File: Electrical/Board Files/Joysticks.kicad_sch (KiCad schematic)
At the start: 8 parts

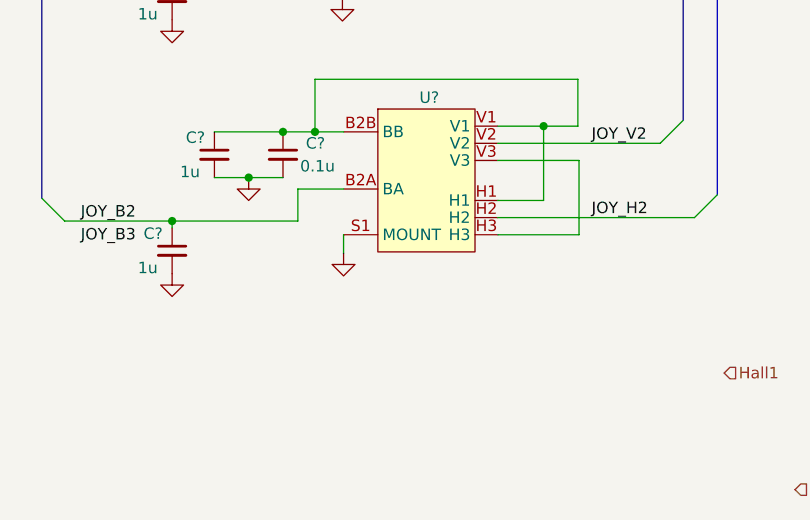
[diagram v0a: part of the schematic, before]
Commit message: Adding new block diagram
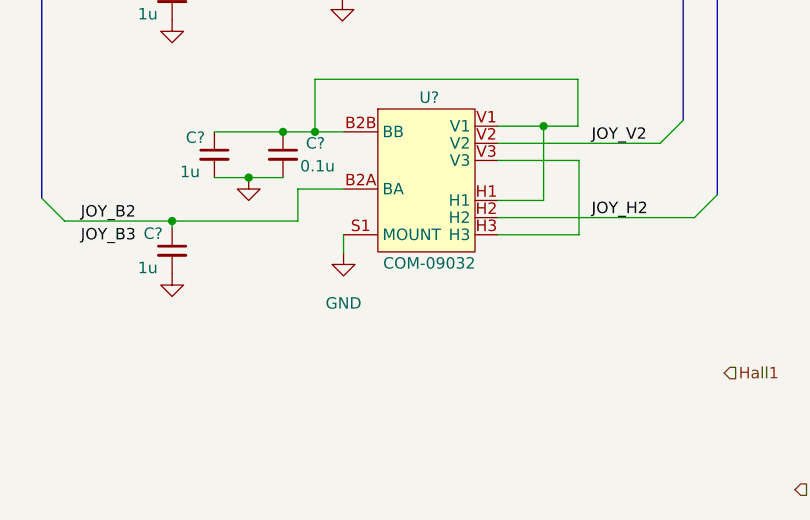
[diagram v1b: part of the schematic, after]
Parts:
- U?: value (none) -> COM-09032
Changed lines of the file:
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@@
       (effects (font (size 1.27 1.27)) hide)
     )
-    (property "Value" "" (id 1) (at 142.621 117.475 0))
+    (property "Value" "GND" (id 1) (at 142.621 117.475 0))
     (property "Footprint" "" (id 2) (at 142.621 111.887 0)
       (effects (font (size 1.27 1.27)) hide)
@@
     (in_bom yes) (on_board yes)
     (property "Reference" "U?" (id 0) (at 152.146 94.615 0))
-    (property "Value" "" (id 1) (at 152.146 113.03 0))
+    (property "Value" "COM-09032" (id 1) (at 152.146 113.03 0))
     (property "Footprint" "" (id 2) (at 152.146 102.87 0)
       (effects (font (size 1.27 1.27)) hide)

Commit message: Updating for 3v3 operation
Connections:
- net GND: now also U?.H3, U?.H3, U?.V3, U?.V3
- net +3V3: now reaches C?.1, C?.1, U?.B1B (S1), U?.B2B (BB), U?.H1, U?.V1
- net +3V3: now also C?.1, C?.1, U?.B1B (S1), U?.B2B (BB), U?.H1, U?.V1
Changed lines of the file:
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@@
   (junction (at 164.719 69.469) (diameter 0) (color 0 0 0 0)
   )
+  (junction (at 139.319 64.262) (diameter 0) (color 0 0 0 0)
+  )
+  (junction (at 168.783 109.855) (diameter 0) (color 0 0 0 0)
+  )
   (junction (at 139.446 98.425) (diameter 0) (color 0 0 0 0)
   )
@@
   )
   (junction (at 131.953 75.184) (diameter 0) (color 0 0 0 0)
+  )
+  (junction (at 139.446 92.583) (diameter 0) (color 0 0 0 0)
+  )
+  (junction (at 168.656 81.534) (diameter 0) (color 0 0 0 0)
   )
   (junction (at 135.763 70.104) (diameter 0) (color 0 0 0 0)
@@
     (effects (font (size 1.27 1.27)) (justify left bottom))
   )
-  (label "JOY_B3" (at 113.411 110.871 0)
-    (effects (font (size 1.27 1.27)) (justify left bottom))
-  )
   (label "JOY_V1" (at 170.18 71.374 0)
     (effects (font (size 1.27 1.27)) (justify left bottom))
@@
     (effects (font (size 1.27 1.27)) (justify left bottom))
   )
-  (hierarchical_label "JOY_H[1..2]" (shape input) (at 194.31 77.089 0)
+  (hierarchical_label "JOY_H[1..2]" (shape output) (at 194.31 77.089 0)
     (effects (font (size 1.27 1.27)) (justify left))
   )
-  (hierarchical_label "JOY_V[1..2]" (shape input) (at 194.31 68.834 0)
+  (hierarchical_label "JOY_V[1..2]" (shape output) (at 194.31 68.834 0)
     (effects (font (size 1.27 1.27)) (justify left))
   )
-  (hierarchical_label "hall2" (shape input) (at 192.786 138.176 0)
+  (hierarchical_label "hall2" (shape output) (at 192.786 138.176 0)
     (effects (font (size 1.27 1.27)) (justify left))
   )
-  (hierarchical_label "JOY_B[1..2]" (shape input) (at 106.045 77.47 180)
+  (hierarchical_label "JOY_B[1..2]" (shape output) (at 106.045 77.47 180)
     (effects (font (size 1.27 1.27)) (justify right))
   )
-  (hierarchical_label "Hall1" (shape input) (at 184.912 125.222 0)
+  (hierarchical_label "Hall1" (shape output) (at 184.912 125.222 0)
     (effects (font (size 1.27 1.27)) (justify left))
   )
@@
     (pin "1")
   )
+  (symbol (lib_id "power:+3V3") (at 139.446 92.583 0) (unit 1)
+    (in_bom yes) (on_board yes) (fields_autoplaced)
+    (property "Reference" "#PWR?" (id 0) (at 139.446 96.393 0)
+      (effects (font (size 1.27 1.27)) hide)
+    )
+    (property "Value" "+3V3" (id 1) (at 139.446 88.011 0))
+    (property "Footprint" "" (id 2) (at 139.446 92.583 0)
+      (effects (font (size 1.27 1.27)) hide)
+    )
+    (property "Datasheet" "" (id 3) (at 139.446 92.583 0)
+      (effects (font (size 1.27 1.27)) hide)
+    )
+    (pin "1")
+  )
   (symbol (lib_id "Device:C_Small") (at 123.571 111.633 0) (unit 1)
     (in_bom yes) (on_board yes)
@@
     (pin "2")
   )
+  (symbol (lib_id "power:GND") (at 168.656 81.534 0) (unit 1)
+    (in_bom yes) (on_board yes) (fields_autoplaced)
+    (property "Reference" "#PWR?" (id 0) (at 168.656 87.884 0)
+      (effects (font (size 1.27 1.27)) hide)
+    )
+    (property "Value" "~" (id 1) (at 168.656 87.122 0))
+    (property "Footprint" "" (id 2) (at 168.656 81.534 0)
+      (effects (font (size 1.27 1.27)) hide)
+    )
+    (property "Datasheet" "" (id 3) (at 168.656 81.534 0)
+      (effects (font (size 1.27 1.27)) hide)
+    )
+    (pin "1")
+  )
   (symbol (lib_id "power:GND") (at 123.571 114.173 0) (unit 1)
     (in_bom yes) (on_board yes) (fields_autoplaced)
@@
     (pin "1")
     (pin "2")
+  )
+  (symbol (lib_id "power:GND") (at 168.783 109.855 0) (unit 1)
+    (in_bom yes) (on_board yes) (fields_autoplaced)
+    (property "Reference" "#PWR?" (id 0) (at 168.783 116.205 0)
+      (effects (font (size 1.27 1.27)) hide)
+    )
+    (property "Value" "~" (id 1) (at 168.783 115.443 0))
+    (property "Footprint" "" (id 2) (at 168.783 109.855 0)
+      (effects (font (size 1.27 1.27)) hide)
+    )
+    (property "Datasheet" "" (id 3) (at 168.783 109.855 0)
+      (effects (font (size 1.27 1.27)) hide)
+    )
+    (pin "1")
   )
   (symbol (lib_id "power:GND") (at 142.621 111.887 0) (unit 1)
@@
     (pin "V3")
   )
+  (symbol (lib_id "power:+3V3") (at 139.319 64.262 0) (unit 1)
+    (in_bom yes) (on_board yes) (fields_autoplaced)
+    (property "Reference" "#PWR?" (id 0) (at 139.319 68.072 0)
+      (effects (font (size 1.27 1.27)) hide)
+    )
+    (property "Value" "+3V3" (id 1) (at 139.319 59.69 0))
+    (property "Footprint" "" (id 2) (at 139.319 64.262 0)
+      (effects (font (size 1.27 1.27)) hide)
+    )
+    (property "Datasheet" "" (id 3) (at 139.319 64.262 0)
+      (effects (font (size 1.27 1.27)) hide)
+    )
+    (pin "1")
+  )
 )

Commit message: Added buzz and vibe, moved SPI, added 2 LEDs
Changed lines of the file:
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@@
     (effects (font (size 1.27 1.27)) (justify left))
   )
-  (hierarchical_label "hall2" (shape output) (at 192.786 138.176 0)
+  (hierarchical_label "HALL2" (shape output) (at 192.786 138.176 0)
     (effects (font (size 1.27 1.27)) (justify left))
   )
@@
     (effects (font (size 1.27 1.27)) (justify right))
   )
-  (hierarchical_label "Hall1" (shape output) (at 184.912 125.222 0)
+  (hierarchical_label "HALL1" (shape output) (at 184.912 125.222 0)
     (effects (font (size 1.27 1.27)) (justify left))
   )

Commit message: Added Xbee libs and bus aliases
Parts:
- gave numbers to parts that had none: 8
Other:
- title: (none) -> Robotics Controller
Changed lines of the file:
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@@
 (kicad_sch (version 20211123) (generator eeschema)
   (paper "A4")
+  (title_block
+    (title "Robotics Controller")
+    (rev "A")
+  )
   (junction (at 164.846 69.469) (diameter 0) (color 0 0 0 0)
   )
@@
     (stroke (width 0) (type default) (color 0 0 0 0))
   )
+  (bus_entry (at 89.535 130.048) (size 2.54 2.54)
+    (stroke (width 0) (type default) (color 0 0 0 0))
+  )
+  (bus_entry (at 95.631 130.175) (size 2.54 2.54)
+    (stroke (width 0) (type default) (color 0 0 0 0))
+  )
   (wire (pts (xy 139.446 92.583) (xy 139.446 98.425))
     (stroke (width 0) (type default) (color 0 0 0 0))
@@
     (stroke (width 0) (type default) (color 0 0 0 0))
   )
+  (wire (pts (xy 92.075 132.588) (xy 92.075 135.509))
+    (stroke (width 0) (type default) (color 0 0 0 0))
+  )
   (wire (pts (xy 164.846 77.724) (xy 164.846 69.469))
     (stroke (width 0) (type default) (color 0 0 0 0))
@@
     (stroke (width 0) (type default) (color 0 0 0 0))
   )
+  (bus (pts (xy 95.631 130.175) (xy 106.045 130.175))
+    (stroke (width 0) (type default) (color 0 0 0 0))
+  )
   (wire (pts (xy 168.529 64.262) (xy 168.529 69.469))
     (stroke (width 0) (type default) (color 0 0 0 0))
@@
     (stroke (width 0) (type default) (color 0 0 0 0))
   )
+  (bus (pts (xy 82.423 130.175) (xy 95.631 130.175))
+    (stroke (width 0) (type default) (color 0 0 0 0))
+  )
   (wire (pts (xy 142.494 81.534) (xy 142.494 83.566))
     (stroke (width 0) (type default) (color 0 0 0 0))
@@
     (stroke (width 0) (type default) (color 0 0 0 0))
   )
+  (wire (pts (xy 98.171 132.715) (xy 98.806 132.715))
+    (stroke (width 0) (type default) (color 0 0 0 0))
+  )
   (wire (pts (xy 137.541 104.775) (xy 142.621 104.775))
     (stroke (width 0) (type default) (color 0 0 0 0))
@@
     (stroke (width 0) (type default) (color 0 0 0 0))
   )
+  (label "HALL2" (at 92.075 135.509 0)
+    (effects (font (size 1.27 1.27)) (justify left bottom))
+  )
   (label "JOY_B1" (at 113.411 80.01 0)
     (effects (font (size 1.27 1.27)) (justify left bottom))
@@
   )
   (label "JOY_H1" (at 170.18 79.629 0)
+    (effects (font (size 1.27 1.27)) (justify left bottom))
+  )
+  (label "HALL1" (at 98.806 132.715 0)
     (effects (font (size 1.27 1.27)) (justify left bottom))
   )
@@
     (effects (font (size 1.27 1.27)) (justify left))
   )
-  (hierarchical_label "HALL2" (shape output) (at 192.786 138.176 0)
+  (hierarchical_label "HALL[1..2]" (shape input) (at 106.045 130.175 0)
     (effects (font (size 1.27 1.27)) (justify left))
   )
@@
     (effects (font (size 1.27 1.27)) (justify right))
   )
-  (hierarchical_label "HALL1" (shape output) (at 184.912 125.222 0)
-    (effects (font (size 1.27 1.27)) (justify left))
-  )
   (symbol (lib_id "power:GND") (at 132.08 103.505 0) (unit 1)
     (in_bom yes) (on_board yes) (fields_autoplaced)
-    (property "Reference" "#PWR?" (id 0) (at 132.08 109.855 0)
+    (property "Reference" "#PWR023" (id 0) (at 132.08 109.855 0)
       (effects (font (size 1.27 1.27)) hide)
     )
@@
   (symbol (lib_id "power:GND") (at 131.953 75.184 0) (unit 1)
     (in_bom yes) (on_board yes) (fields_autoplaced)
-    (property "Reference" "#PWR?" (id 0) (at 131.953 81.534 0)
+    (property "Reference" "#PWR022" (id 0) (at 131.953 81.534 0)
       (effects (font (size 1.27 1.27)) hide)
     )
@@
   (symbol (lib_id "power:+3V3") (at 139.446 92.583 0) (unit 1)
     (in_bom yes) (on_board yes) (fields_autoplaced)
-    (property "Reference" "#PWR?" (id 0) (at 139.446 96.393 0)
+    (property "Reference" "#PWR025" (id 0) (at 139.446 96.393 0)
       (effects (font (size 1.27 1.27)) hide)
     )
@@
   (symbol (lib_id "Device:C_Small") (at 123.571 111.633 0) (unit 1)
     (in_bom yes) (on_board yes)
-    (property "Reference" "C?" (id 0) (at 120.396 109.728 0)
+    (property "Reference" "C28" (id 0) (at 120.396 109.728 0)
       (effects (font (size 1.27 1.27)) (justify left))
     )
@@
   (symbol (lib_id "power:GND") (at 142.494 83.566 0) (unit 1)
     (in_bom yes) (on_board yes) (fields_autoplaced)
-    (property "Reference" "#PWR?" (id 0) (at 142.494 89.916 0)
+    (property "Reference" "#PWR026" (id 0) (at 142.494 89.916 0)
       (effects (font (size 1.27 1.27)) hide)
     )
@@
   (symbol (lib_id "Device:C_Small") (at 128.27 100.965 0) (unit 1)
     (in_bom yes) (on_board yes)
-    (property "Reference" "C?" (id 0) (at 125.095 99.06 0)
+    (property "Reference" "C30" (id 0) (at 125.095 99.06 0)
       (effects (font (size 1.27 1.27)) (justify left))
     )
@@
   (symbol (lib_id "power:GND") (at 168.656 81.534 0) (unit 1)
     (in_bom yes) (on_board yes) (fields_autoplaced)
-    (property "Reference" "#PWR?" (id 0) (at 168.656 87.884 0)
+    (property "Reference" "#PWR028" (id 0) (at 168.656 87.884 0)
       (effects (font (size 1.27 1.27)) hide)
     )
@@
   (symbol (lib_id "power:GND") (at 123.571 114.173 0) (unit 1)
     (in_bom yes) (on_board yes) (fields_autoplaced)
-    (property "Reference" "#PWR?" (id 0) (at 123.571 120.523 0)
+    (property "Reference" "#PWR021" (id 0) (at 123.571 120.523 0)
       (effects (font (size 1.27 1.27)) hide)
     )
@@
   (symbol (lib_id "Device:C_Small") (at 135.763 72.644 0) (unit 1)
     (in_bom yes) (on_board yes)
-    (property "Reference" "C?" (id 0) (at 138.303 71.374 0)
+    (property "Reference" "C31" (id 0) (at 138.303 71.374 0)
       (effects (font (size 1.27 1.27)) (justify left))
     )
@@
   (symbol (lib_id "Device:C_Small") (at 123.571 83.439 0) (unit 1)
     (in_bom yes) (on_board yes)
-    (property "Reference" "C?" (id 0) (at 120.396 81.534 0)
+    (property "Reference" "C27" (id 0) (at 120.396 81.534 0)
       (effects (font (size 1.27 1.27)) (justify left))
     )
@@
   (symbol (lib_id "power:GND") (at 168.783 109.855 0) (unit 1)
     (in_bom yes) (on_board yes) (fields_autoplaced)
-    (property "Reference" "#PWR?" (id 0) (at 168.783 116.205 0)
+    (property "Reference" "#PWR029" (id 0) (at 168.783 116.205 0)
       (effects (font (size 1.27 1.27)) hide)
     )
@@
   (symbol (lib_id "power:GND") (at 142.621 111.887 0) (unit 1)
     (in_bom yes) (on_board yes) (fields_autoplaced)
-    (property "Reference" "#PWR?" (id 0) (at 142.621 118.237 0)
+    (property "Reference" "#PWR027" (id 0) (at 142.621 118.237 0)
       (effects (font (size 1.27 1.27)) hide)
     )
@@
   (symbol (lib_id "power:GND") (at 123.571 85.979 0) (unit 1)
     (in_bom yes) (on_board yes) (fields_autoplaced)
-    (property "Reference" "#PWR?" (id 0) (at 123.571 92.329 0)
+    (property "Reference" "#PWR020" (id 0) (at 123.571 92.329 0)
       (effects (font (size 1.27 1.27)) hide)
     )
@@
   (symbol (lib_id "Device:C_Small") (at 135.89 100.965 0) (unit 1)
     (in_bom yes) (on_board yes)
-    (property "Reference" "C?" (id 0) (at 138.43 99.695 0)
+    (property "Reference" "C32" (id 0) (at 138.43 99.695 0)
       (effects (font (size 1.27 1.27)) (justify left))
     )
@@
   (symbol (lib_id "Controller:COM-09032") (at 152.146 102.87 0) (unit 1)
     (in_bom yes) (on_board yes)
-    (property "Reference" "U?" (id 0) (at 152.146 94.615 0))
+    (property "Reference" "U6" (id 0) (at 152.146 94.615 0))
     (property "Value" "COM-09032" (id 1) (at 152.146 113.03 0))
     (property "Footprint" "" (id 2) (at 152.146 102.87 0)
@@
   (symbol (lib_id "Device:C_Small") (at 128.143 72.644 0) (unit 1)
     (in_bom yes) (on_board yes)
-    (property "Reference" "C?" (id 0) (at 124.968 70.739 0)
+    (property "Reference" "C29" (id 0) (at 124.968 70.739 0)
       (effects (font (size 1.27 1.27)) (justify left))
     )
@@
   (symbol (lib_id "Controller:COM-09032") (at 152.019 74.549 0) (unit 1)
     (in_bom yes) (on_board yes)
-    (property "Reference" "U?" (id 0) (at 152.019 66.294 0))
+    (property "Reference" "U5" (id 0) (at 152.019 66.294 0))
     (property "Value" "~" (id 1) (at 152.019 84.709 0))
     (property "Footprint" "" (id 2) (at 152.019 74.549 0)
@@
   (symbol (lib_id "power:+3V3") (at 139.319 64.262 0) (unit 1)
     (in_bom yes) (on_board yes) (fields_autoplaced)
-    (property "Reference" "#PWR?" (id 0) (at 139.319 68.072 0)
-      (effects (font (size 1.27 1.27)) hide)
-    )
+    (property "Reference" "#PWR024" (id 0) (at 139.319 68.072 0)
+      (effects (font (size 1.27 1.27)) hide)
+    )

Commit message: Added hall effect sensors
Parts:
- added C37, C39: 1u, symbol Device:C_Small
- added C38, C40: 0.01u, symbol Device:C_Small
- added U10, U9: DRV5055A2xLPGxQ1, Package_TO_SOT_THT:TO-92_Inline, symbol Sensor_Magnetic:DRV5055A2xLPGxQ1
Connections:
- net +3V3: now also C37.1, C38.1, C39.1, C40.1, U10.1 (VCC), U9.1 (VCC)
- net GND: now also C37.2, C38.2, C39.2, C40.2, U10.2 (GND), U9.2 (GND)
- net HALL1: now also U9.3 (OUT)
- net HALL2: now also U10.3 (OUT)

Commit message: Updating title block fields and adding pdf schematic
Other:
- company: (none) -> Rockerbotics
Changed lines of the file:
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@@
   (title_block
     (title "Robotics Controller")
+    (date "2022-09-02")
     (rev "A")
+    (company "Rockerbotics")
   )
   (junction (at 164.846 69.469) (diameter 0) (color 0 0 0 0)
